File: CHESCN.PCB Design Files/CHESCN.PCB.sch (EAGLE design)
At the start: 78 parts, among them U2 MAX232SOIC16, U3 RS485SOIC

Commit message: Pre-fab, added headers
Need to export production files
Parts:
- added JP1, JP2: (no value), SparkFun:M02POGO_PIN_HOLES_ONLY
- added U$38: 10k, GW-devices:RF-R0402
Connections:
- net +3V3: now also U$38.2
- net GND: now also JP1.2, JP2.2
- net N$60: now also JP2.1, U$38.1
- net V+: now also JP1.1
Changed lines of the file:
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@@
 <?xml version="1.0" encoding="utf-8"?>
 <!DOCTYPE eagle SYSTEM "eagle.dtd">
-<eagle version="6.6.0">
+<eagle version="6.5.0">
 <drawing>
 <settings>
@@
 </part>
 <part name="P+9" library="supply1" deviceset="+5V" device=""/>
+<part name="U$38" library="GW-devices" deviceset="RF-R" device="0402" value="10k"/>
+<part name="GND28" library="supply1" deviceset="GND" device=""/>
+<part name="JP2" library="SparkFun" deviceset="M02" device="POGO_PIN_HOLES_ONLY"/>
+<part name="JP1" library="SparkFun" deviceset="M02" device="POGO_PIN_HOLES_ONLY"/>
 </parts>
 <sheets>
@@
 </instance>
 <instance part="P+9" gate="1" x="-58.42" y="111.76"/>
+<instance part="U$38" gate="&gt;NAME" x="-464.82" y="165.1" rot="R180"/>
+<instance part="GND28" gate="1" x="-457.2" y="172.72"/>
+<instance part="JP2" gate="G$1" x="-459.74" y="187.96" rot="R270"/>
+<instance part="JP1" gate="G$1" x="106.68" y="193.04" rot="R270"/>
 </instances>
 <busses>
@@
 <pinref part="+3V3" gate="G$1" pin="+3V3"/>
 <wire x1="-487.68" y1="162.56" x2="-474.98" y2="162.56" width="0.1524" layer="91"/>
-<wire x1="-474.98" y1="162.56" x2="-474.98" y2="167.64" width="0.1524" layer="91"/>
+<wire x1="-474.98" y1="162.56" x2="-474.98" y2="165.1" width="0.1524" layer="91"/>
+<pinref part="U$38" gate="&gt;NAME" pin="2"/>
+<wire x1="-474.98" y1="165.1" x2="-474.98" y2="167.64" width="0.1524" layer="91"/>
+<wire x1="-469.9" y1="165.1" x2="-474.98" y2="165.1" width="0.1524" layer="91"/>
+<junction x="-474.98" y="165.1"/>
 </segment>
 </net>
@@
 <wire x1="114.3" y1="170.18" x2="114.3" y2="172.72" width="0.1524" layer="91"/>
 <pinref part="GND3" gate="1" pin="GND"/>
-<wire x1="114.3" y1="172.72" x2="104.14" y2="172.72" width="0.1524" layer="91"/>
+<wire x1="114.3" y1="172.72" x2="109.22" y2="172.72" width="0.1524" layer="91"/>
 <pinref part="U$9" gate="G$1" pin="GND"/>
+<pinref part="JP1" gate="G$1" pin="2"/>
+<wire x1="109.22" y1="172.72" x2="104.14" y2="172.72" width="0.1524" layer="91"/>
+<wire x1="109.22" y1="185.42" x2="109.22" y2="172.72" width="0.1524" layer="91"/>
+<junction x="109.22" y="172.72"/>
 </segment>
 <segment>
@@
 <junction x="-35.56" y="114.3"/>
 </segment>
+<segment>
+<pinref part="GND28" gate="1" pin="GND"/>
+<wire x1="-457.2" y1="175.26" x2="-457.2" y2="180.34" width="0.1524" layer="91"/>
+<pinref part="JP2" gate="G$1" pin="2"/>
+</segment>
 </net>
 <net name="V+" class="0">
@@
 <junction x="109.22" y="165.1"/>
 <pinref part="SUPPLY1" gate="1" pin="V+"/>
-<wire x1="93.98" y1="175.26" x2="93.98" y2="165.1" width="0.1524" layer="91"/>
+<wire x1="93.98" y1="175.26" x2="93.98" y2="172.72" width="0.1524" layer="91"/>
+<wire x1="93.98" y1="172.72" x2="93.98" y2="165.1" width="0.1524" layer="91"/>
 <wire x1="93.98" y1="165.1" x2="99.06" y2="165.1" width="0.1524" layer="91"/>
 <pinref part="U$33" gate="G$1" pin="2"/>
@@
 <pinref part="U$34" gate="G$1" pin="2"/>
 <junction x="104.14" y="165.1"/>
+<wire x1="93.98" y1="172.72" x2="99.06" y2="172.72" width="0.1524" layer="91"/>
+<wire x1="99.06" y1="172.72" x2="99.06" y2="185.42" width="0.1524" layer="91"/>
+<junction x="93.98" y="172.72"/>
+<pinref part="JP1" gate="G$1" pin="1"/>
+<wire x1="99.06" y1="185.42" x2="106.68" y2="185.42" width="0.1524" layer="91"/>
 </segment>
 <segment>
@@
 <segment>
 <pinref part="U$26" gate="G$1" pin="TRIG"/>
-<wire x1="-487.68" y1="157.48" x2="-457.2" y2="157.48" width="0.1524" layer="91"/>
+<wire x1="-487.68" y1="157.48" x2="-459.74" y2="157.48" width="0.1524" layer="91"/>
+<wire x1="-459.74" y1="157.48" x2="-457.2" y2="157.48" width="0.1524" layer="91"/>
 <wire x1="-457.2" y1="157.48" x2="-457.2" y2="127" width="0.1524" layer="91"/>
 <pinref part="U$10" gate="G$1" pin="PTE4/LLWU_P2/SPI1_PCS0/MTRACE_D0"/>
 <wire x1="-449.58" y1="127" x2="-457.2" y2="127" width="0.1524" layer="91"/>
 <wire x1="-190.5" y1="127" x2="-449.58" y2="127" width="0.1524" layer="91"/>
-</segment>
-</net>
+<wire x1="-459.74" y1="157.48" x2="-459.74" y2="165.1" width="0.1524" layer="91"/>
+<junction x="-459.74" y="157.48"/>
+<pinref part="U$38" gate="&gt;NAME" pin="1"/>
+<wire x1="-459.74" y1="165.1" x2="-459.74" y2="180.34" width="0.1524" layer="91"/>
+<junction x="-459.74" y="165.1"/>
+<pinref part="JP2" gate="G$1" pin="1"/>
+</segment>
+</net>

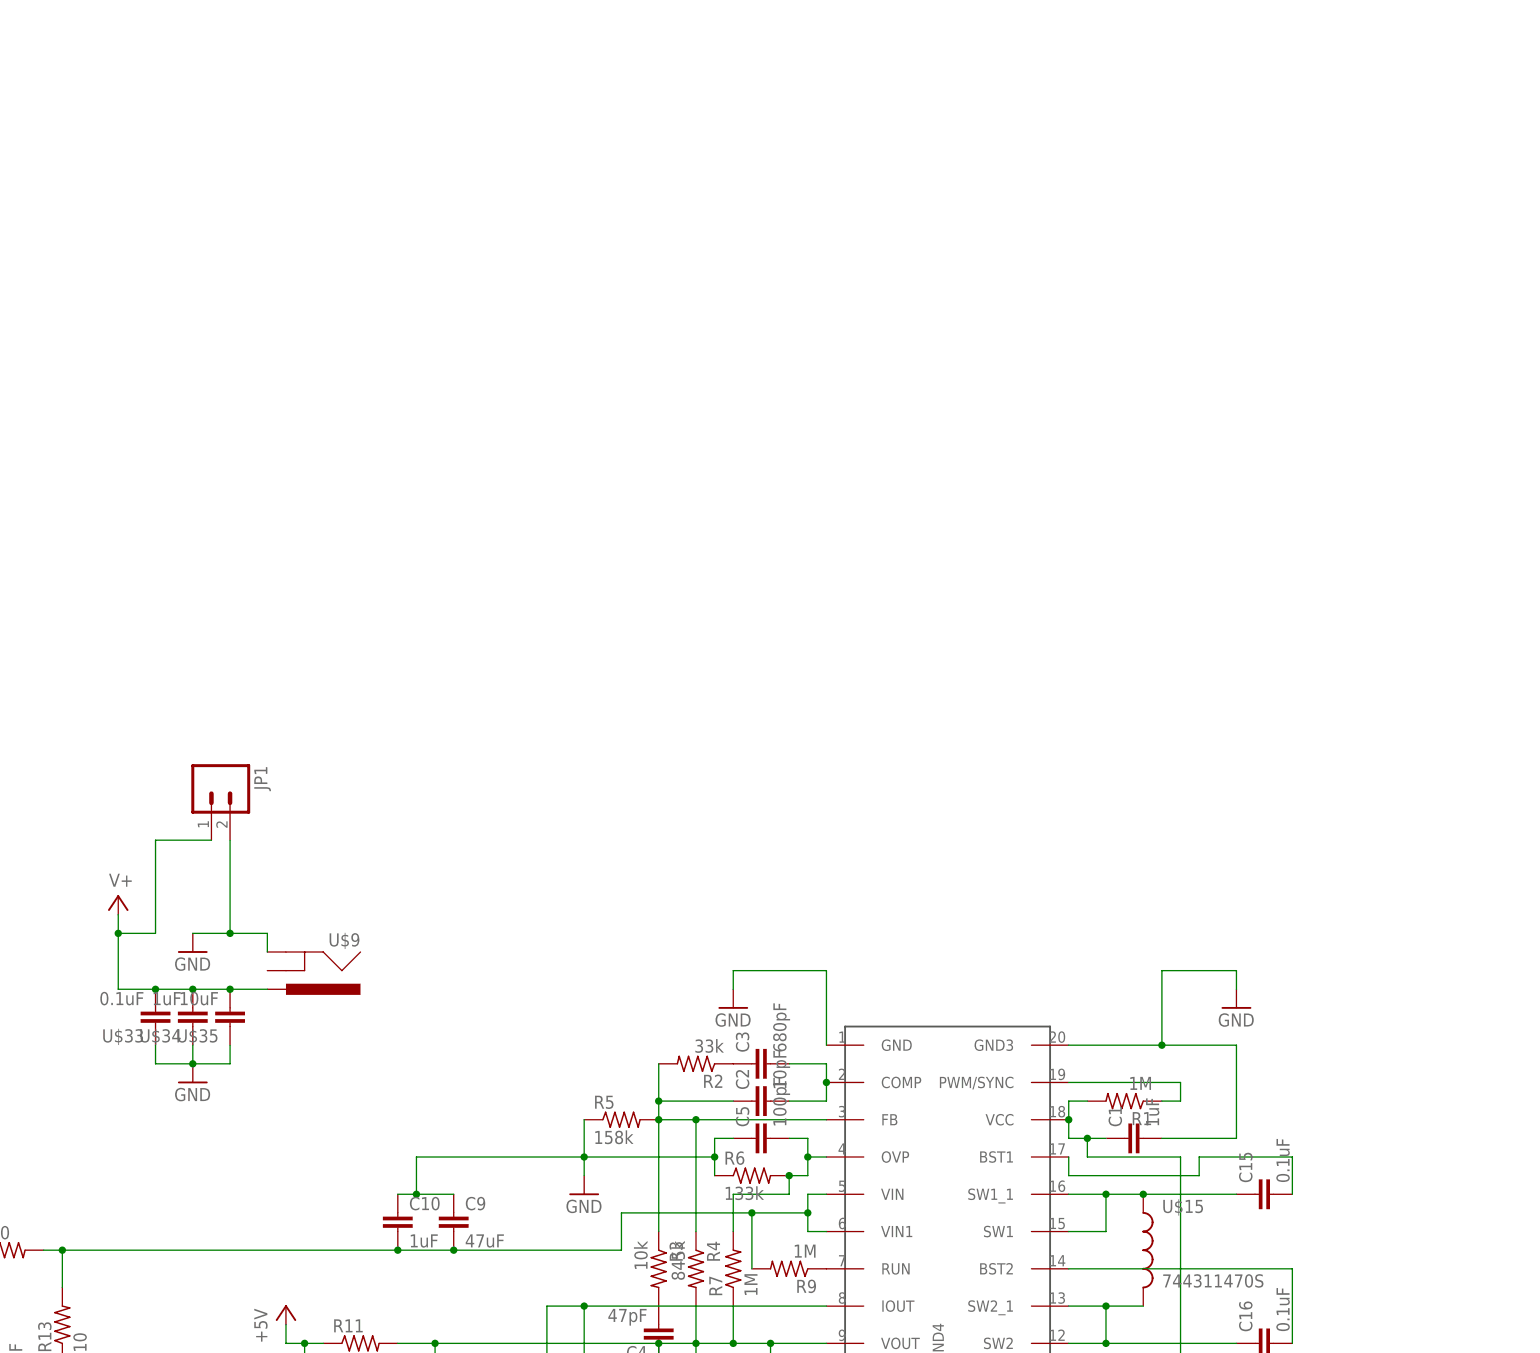
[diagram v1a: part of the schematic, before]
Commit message: Various fixes + BL board
Fixed consistency issues (diode, inductor), added laser test files and
added backlight board
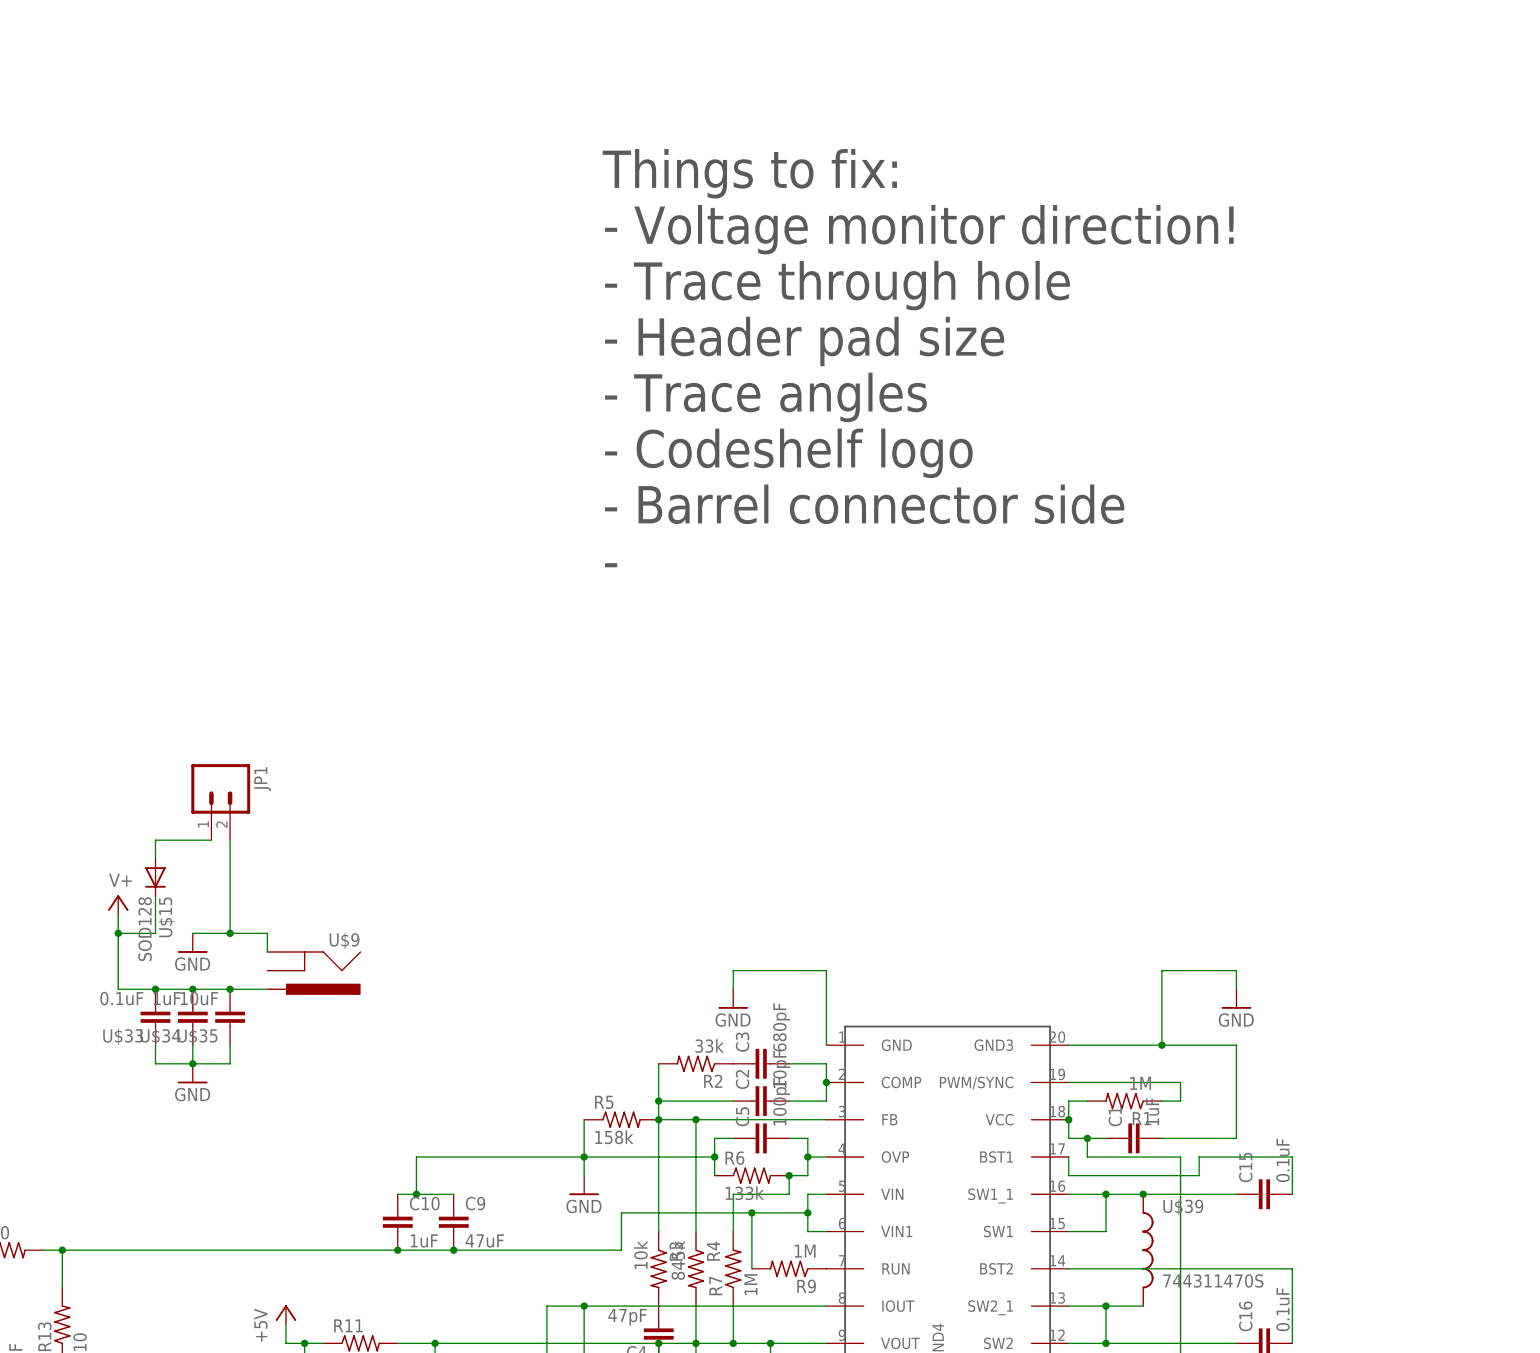
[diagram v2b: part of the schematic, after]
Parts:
- added U$39: 744311470S, KW2:744311470S
- U$15: value 744311470S -> SOD128; device KW2:744311470S -> KW2:SOD128
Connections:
- new net N$65: JP1.1, U$15.A
- net N$32: now also U$39.1; no longer U$15.1
- net N$35: now also U$39.2; no longer U$15.2
- net V+: now also U$15.C; no longer JP1.1
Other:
- note added: "Things to fix: - Voltage monitor direction! - Trace through hole - Header pad size - Trace angles - Codeshelf logo - Barrel connector side -"
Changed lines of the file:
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@@
 <?xml version="1.0" encoding="utf-8"?>
 <!DOCTYPE eagle SYSTEM "eagle.dtd">
-<eagle version="6.5.0">
+<eagle version="6.6.0">
 <drawing>
 <settings>
@@
 <part name="C13" library="GW-devices" deviceset="RF-C" device="0402" value="0.1uF"/>
 <part name="C14" library="GW-devices" deviceset="RF-C" device="0402" value="0.1uF"/>
-<part name="U$15" library="KW2" deviceset="744311470" device="S" value="744311470S"/>
 <part name="C15" library="GW-devices" deviceset="RF-C" device="0402" value="0.1uF"/>
 <part name="C16" library="GW-devices" deviceset="RF-C" device="0402" value="0.1uF"/>
@@
 <part name="JP2" library="SparkFun" deviceset="M02" device="POGO_PIN_HOLES_ONLY"/>
 <part name="JP1" library="SparkFun" deviceset="M02" device="POGO_PIN_HOLES_ONLY"/>
+<part name="U$15" library="KW2" deviceset="SOD128" device=""/>
+<part name="U$39" library="KW2" deviceset="744311470" device="S"/>
 </parts>
 <sheets>
 <sheet>
 <plain>
+<text x="160.02" y="220.98" size="5.08" layer="97">Things to fix:
+- Voltage monitor direction!
+- Trace through hole
+- Header pad size
+- Trace angles
+- Codeshelf logo
+- Barrel connector side
+- </text>
 </plain>
 <instances>
@@
 <instance part="C13" gate="G$1" x="106.68" y="68.58" rot="R270"/>
 <instance part="C14" gate="G$1" x="63.5" y="68.58" rot="R270"/>
-<instance part="U$15" gate="G$1" x="233.68" y="129.54"/>
 <instance part="C15" gate="G$1" x="248.92" y="137.16" rot="R90"/>
 <instance part="C16" gate="G$1" x="248.92" y="116.84" rot="R90"/>
@@
 <instance part="JP2" gate="G$1" x="-459.74" y="187.96" rot="R270"/>
 <instance part="JP1" gate="G$1" x="106.68" y="193.04" rot="R270"/>
+<instance part="U$15" gate="G$1" x="99.06" y="180.34" rot="R270"/>
+<instance part="U$39" gate="G$1" x="233.68" y="129.54"/>
 </instances>
 <busses>
@@
 <junction x="104.14" y="165.1"/>
 <wire x1="93.98" y1="172.72" x2="99.06" y2="172.72" width="0.1524" layer="91"/>
-<wire x1="99.06" y1="172.72" x2="99.06" y2="185.42" width="0.1524" layer="91"/>
 <junction x="93.98" y="172.72"/>
-<pinref part="JP1" gate="G$1" pin="1"/>
-<wire x1="99.06" y1="185.42" x2="106.68" y2="185.42" width="0.1524" layer="91"/>
+<pinref part="U$15" gate="G$1" pin="C"/>
+<wire x1="99.06" y1="177.8" x2="99.06" y2="172.72" width="0.1524" layer="91"/>
 </segment>
 <segment>
@@
 <pinref part="U$44" gate="G$1" pin="SW1"/>
 <wire x1="228.6" y1="132.08" x2="223.52" y2="132.08" width="0.1524" layer="91"/>
-<pinref part="U$15" gate="G$1" pin="1"/>
 <wire x1="233.68" y1="137.16" x2="228.6" y2="137.16" width="0.1524" layer="91"/>
 <junction x="228.6" y="137.16"/>
 <pinref part="C15" gate="G$1" pin="1"/>
 <wire x1="246.38" y1="137.16" x2="233.68" y2="137.16" width="0.1524" layer="91"/>
+<pinref part="U$39" gate="G$1" pin="1"/>
 <junction x="233.68" y="137.16"/>
 </segment>
@@
 <pinref part="U$44" gate="G$1" pin="SW2"/>
 <wire x1="228.6" y1="116.84" x2="223.52" y2="116.84" width="0.1524" layer="91"/>
-<pinref part="U$15" gate="G$1" pin="2"/>
 <wire x1="228.6" y1="121.92" x2="233.68" y2="121.92" width="0.1524" layer="91"/>
 <junction x="228.6" y="121.92"/>
@@
 <wire x1="246.38" y1="116.84" x2="228.6" y2="116.84" width="0.1524" layer="91"/>
 <junction x="228.6" y="116.84"/>
+<pinref part="U$39" gate="G$1" pin="2"/>
 </segment>
 </net>
@@
 </segment>
 </net>
+<net name="N$65" class="0">
+<segment>
+<pinref part="JP1" gate="G$1" pin="1"/>
+<wire x1="99.06" y1="185.42" x2="106.68" y2="185.42" width="0.1524" layer="91"/>
+<pinref part="U$15" gate="G$1" pin="A"/>
+<wire x1="99.06" y1="185.42" x2="99.06" y2="182.88" width="0.1524" layer="91"/>
+</segment>
+</net>
